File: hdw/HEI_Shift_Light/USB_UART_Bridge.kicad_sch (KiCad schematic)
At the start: 27 parts, among them J601 USB_C_Receptacle_USB2.0_16P, U601 FT234XD, U602 ISO7321C

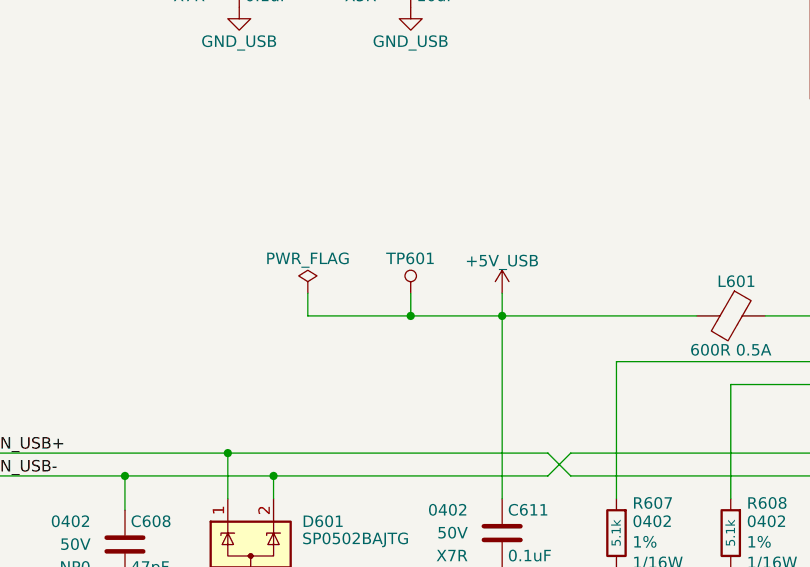
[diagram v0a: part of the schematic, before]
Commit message: arranged components in PCB
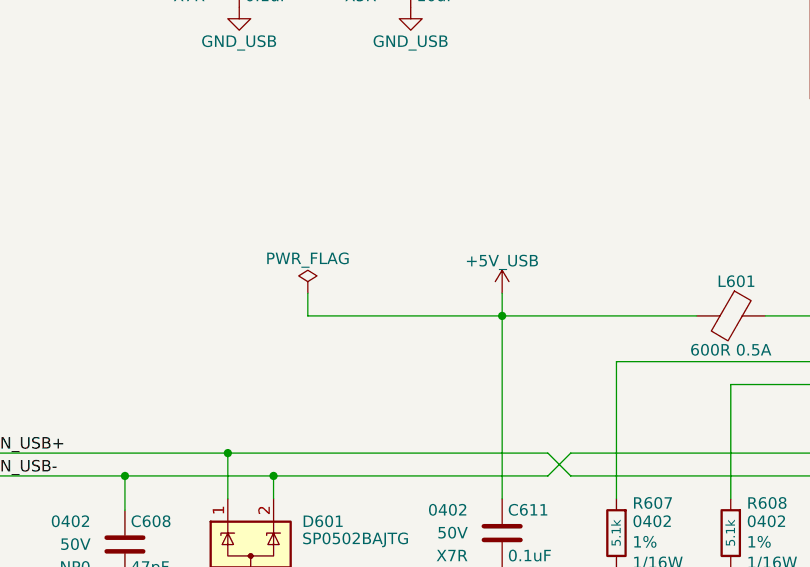
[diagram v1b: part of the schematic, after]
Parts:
- removed TP601: TP, Custom Footprints Library:Test_Point, symbol Custom_Library:TP
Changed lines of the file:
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@@
-	)
-	(junction
-		(at 173.99 91.44)
-		(diameter 0)
-		(color 0 0 0 0)
 	)
 	(junction
@@
 	(wire
 		(pts
-			(xy 162.56 91.44) (xy 173.99 91.44)
+			(xy 162.56 91.44) (xy 184.15 91.44)
 		)
 		(stroke
@@
 	(wire
 		(pts
-			(xy 173.99 91.44) (xy 184.15 91.44)
-		)
-		(stroke
-			(width 0)
-			(type default)
-		)
-	)
-	(wire
-		(pts
 			(xy 247.65 129.54) (xy 247.65 134.62)
 		)
@@
 		(pts
 			(xy 222.25 111.76) (xy 224.79 111.76)
-		)
-		(stroke
-			(width 0)
-			(type default)
-		)
-	)
-	(wire
-		(pts
-			(xy 173.99 88.9) (xy 173.99 91.44)
 		)
 		(stroke
@@
 					(unit 1)
 				)
-			)
-		)
-	)
-	(symbol
-		(lib_id "Custom_Library:TP")
-		(at 173.99 88.9 0)
-		(unit 1)
-		(body_style 1)
-		(exclude_from_sim no)
-		(in_bom yes)
-		(on_board yes)
-		(in_pos_files yes)
-		(dnp no)
-		(property "Reference" "TP601"
-			(at 173.99 85.09 0)
-			(show_name no)
-			(do_not_autoplace no)
-			(effects
-				(font
-					(size 1.27 1.27)
-				)
-			)
-		)
-		(property "Value" "TP"
-			(at 173.99 85.09 0)
-			(hide yes)
-			(show_name no)
-			(do_not_autoplace no)
-			(effects
-				(font
-					(size 1.27 1.27)
-				)
-			)
-		)
-		(property "Footprint" "Custom Footprints Library:Test_Point"
-			(at 173.99 88.9 0)
-			(hide yes)
-			(show_name no)
-			(do_not_autoplace no)
-			(effects
-				(font
-					(size 1.524 1.524)
-				)
-			)
-		)
-		(property "Datasheet" ""
-			(at 173.99 88.9 0)
-			(show_name no)
-			(do_not_autoplace no)
-			(effects
-				(font
-					(size 1.524 1.524)
-				)
-			)
-		)
-		(property "Description" ""
-			(at 173.99 88.9 0)
-			(show_name no)
-			(do_not_autoplace no)
-			(effects
-				(font
-					(size 1.27 1.27)
-				)
-			)
-		)
-		(pin "1"
-		)
-		(instances
-			(project "Analog_Clock"
-				(path "/0dc9b974-a945-4291-bc55-04b8e342b0e5/00000000-0000-0000-0000-00005a0bc776"
-					(reference "TP?")
-					(unit 1)
-				)
-				(path "/0dc9b974-a945-4291-bc55-04b8e342b0e5/00000000-0000-0000-0000-00005a557c58"
-					(reference "TP?")
-					(unit 1)
-				)
-				(path "/0dc9b974-a945-4291-bc55-04b8e342b0e5/00000000-0000-0000-0000-00005cad2d97"
-					(reference "TP?")
-					(unit 1)
-				)
-				(path "/0dc9b974-a945-4291-bc55-04b8e342b0e5/00000000-0000-0000-0000-00005e939f76"
-					(reference "TP?")
-					(unit 1)
-				)
-			)
-			(project "Nixie_Clock_Core"
-				(path "/16fdce21-b570-4d81-a458-e8839d611806/4cb440c2-4356-400c-9387-edaaa635d5a5"
-					(reference "TP1301")
-					(unit 1)
-				)
-			)
-			(project "HEI_Shift_Light"
-				(path "/288c8230-69eb-4ad9-929d-f4630114196f/c4b824f9-827e-4368-b456-592a65eed557"
-					(reference "TP601")
-					(unit 1)
-				)
